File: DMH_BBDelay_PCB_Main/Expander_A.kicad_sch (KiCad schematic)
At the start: 23 parts, among them U27 SSI2162, U28 TL074

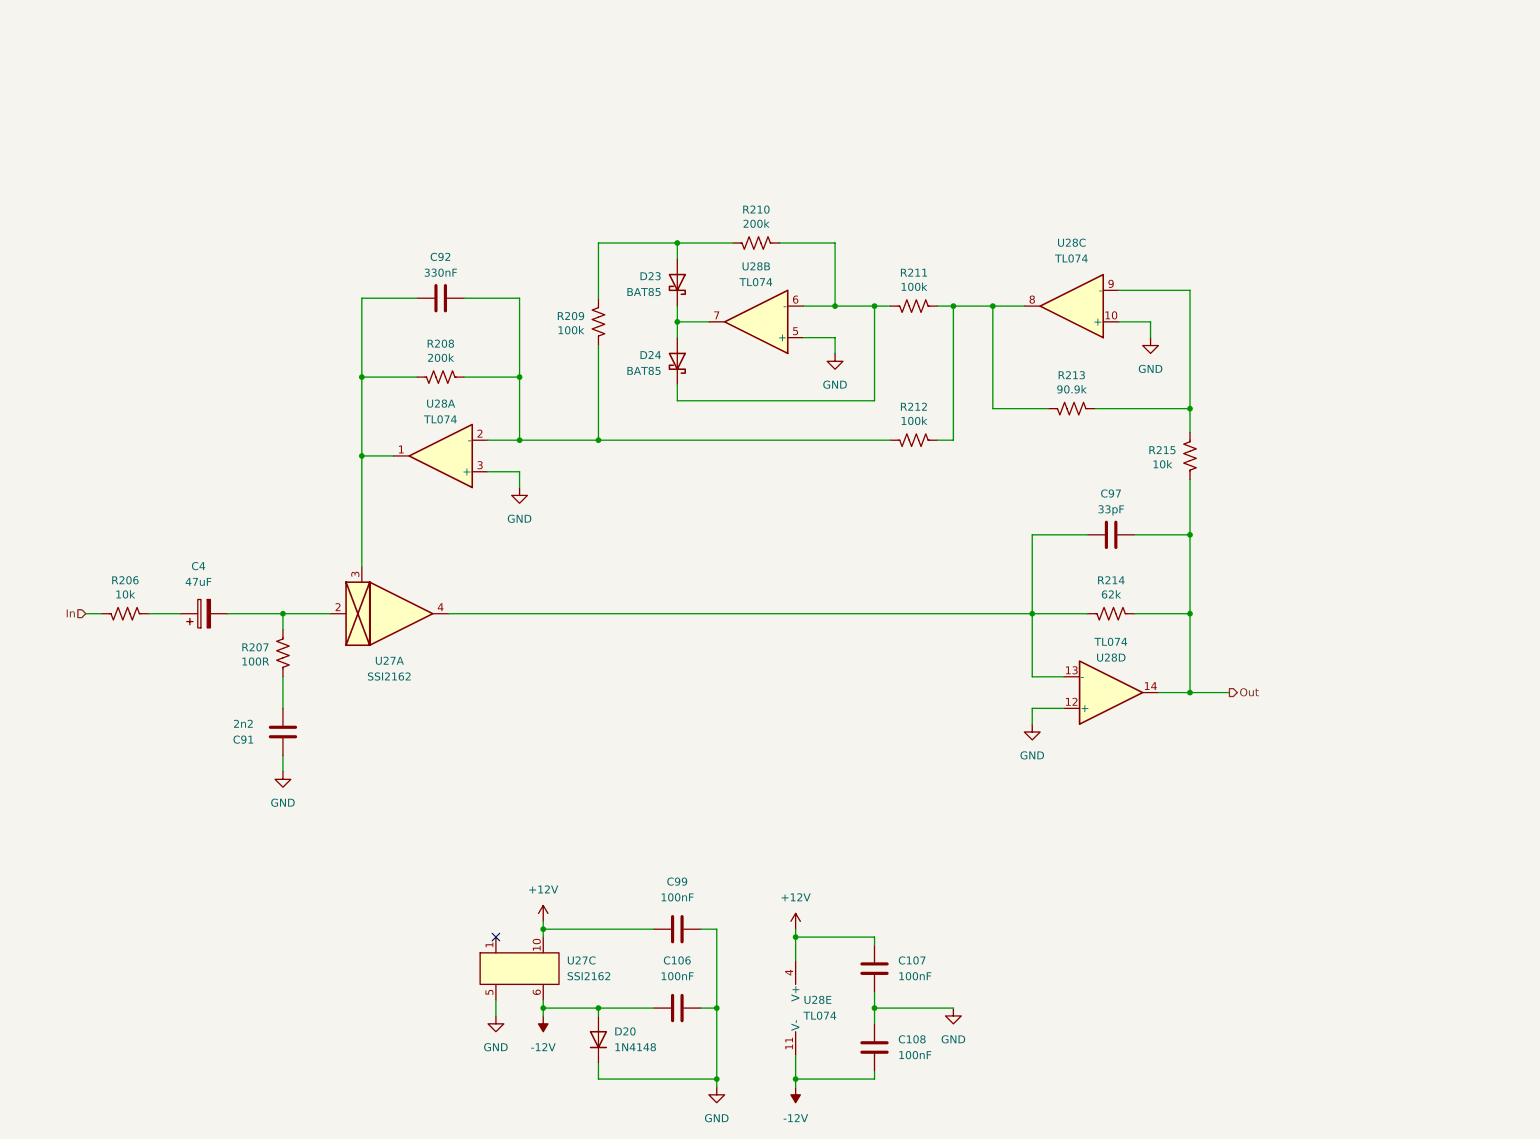
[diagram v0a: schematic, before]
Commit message: Designed Expander circuits
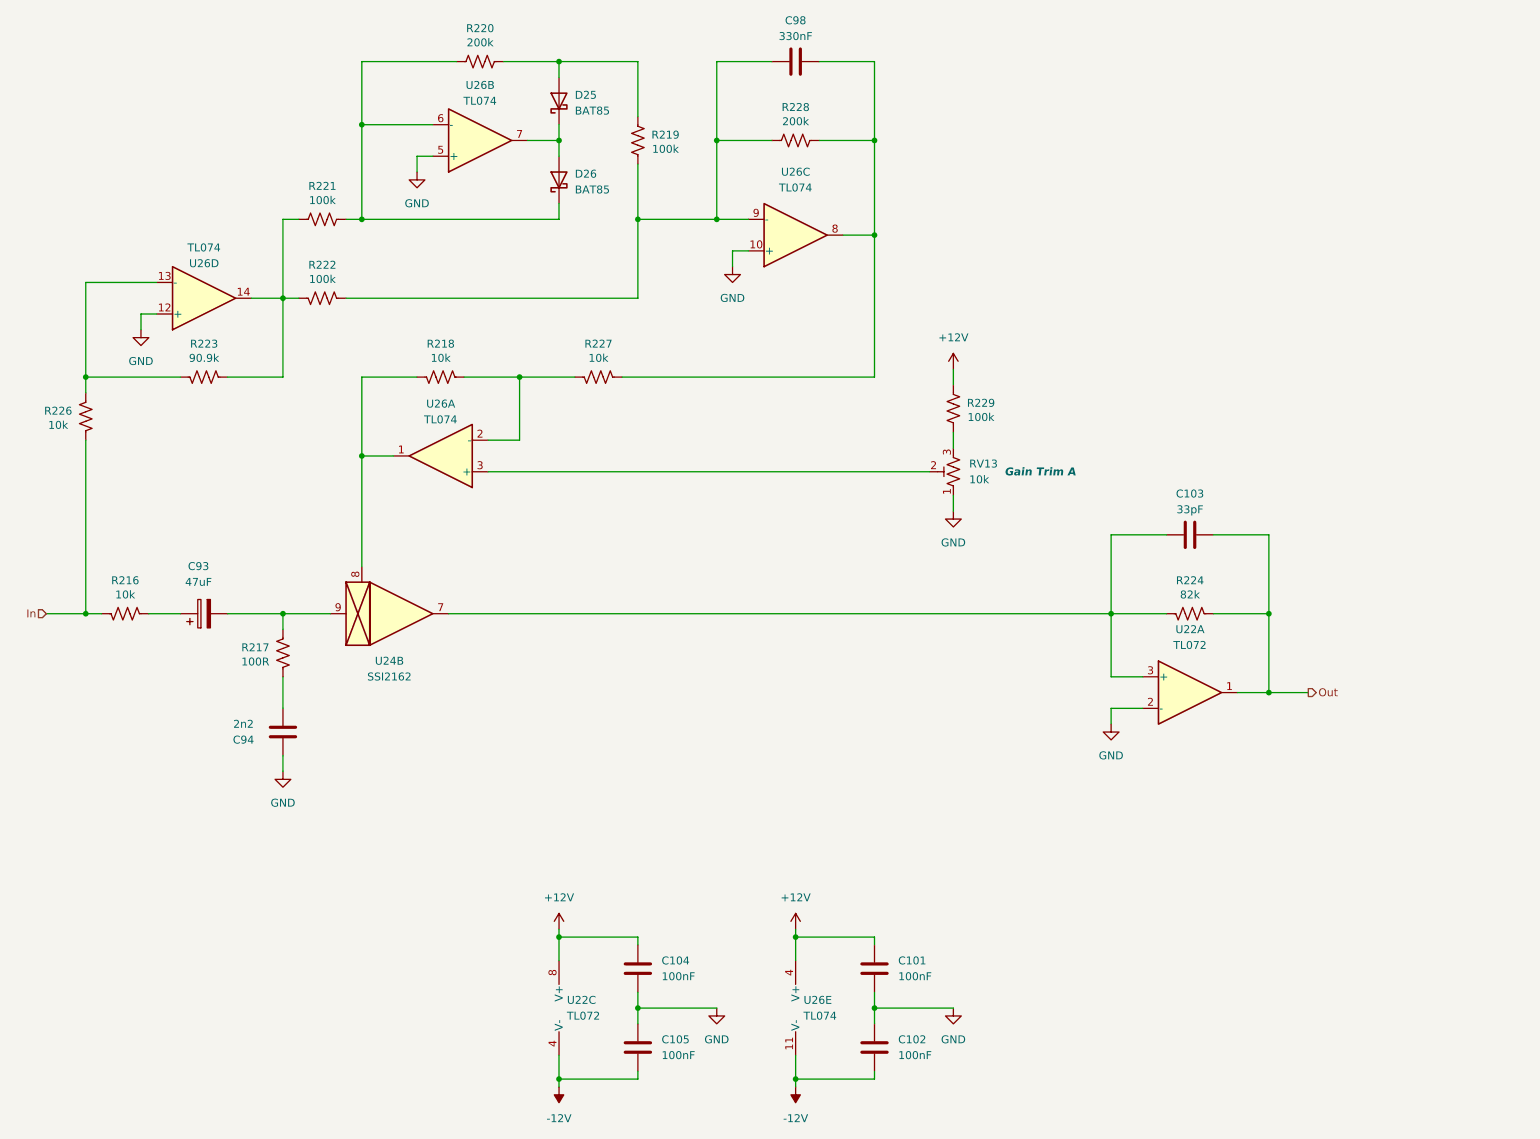
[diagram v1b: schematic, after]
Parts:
- removed C106, C107, C108, C99: 100nF, Capacitor_THT:C_Disc_D4.3mm_W1.9mm_P5.00mm, symbol Device:C
- removed D20: 1N4148, Diode_THT:D_DO-35_SOD27_P7.62mm_Horizontal, symbol Diode:1N4148
- removed R213: 90.9k, Resistor_THT:R_Axial_DIN0207_L6.3mm_D2.5mm_P7.62mm_Horizontal, symbol Device:R_US
- removed R215: 10k, Resistor_THT:R_Axial_DIN0207_L6.3mm_D2.5mm_P7.62mm_Horizontal, symbol Device:R_US
- removed U27: SSI2162, Package_SO:SSOP-10_3.9x4.9mm_P1.00mm, symbol SynthStuff:SSI2162
- removed unit 4 of U28
- added C101, C102, C104, C105: 100nF, Capacitor_THT:C_Disc_D4.3mm_W1.9mm_P5.00mm, symbol Device:C
- added R223: 90.9k, Resistor_THT:R_Axial_DIN0207_L6.3mm_D2.5mm_P7.62mm_Horizontal, symbol Device:R_US
- added R226, R227: 10k, Resistor_THT:R_Axial_DIN0207_L6.3mm_D2.5mm_P7.62mm_Horizontal, symbol Device:R_US
- added R228: 200k, Resistor_THT:R_Axial_DIN0207_L6.3mm_D2.5mm_P7.62mm_Horizontal, symbol Device:R_US
- added R229: 100k, Resistor_THT:R_Axial_DIN0207_L6.3mm_D2.5mm_P7.62mm_Horizontal, symbol Device:R_US
- added RV13: 10k, Potentiometer_THT:Potentiometer_Bourns_3296X_Horizontal, symbol Device:R_Potentiometer_Trim_US
- added U22: TL072, Package_DIP:DIP-8_W7.62mm_Socket, symbol Amplifier_Operational:TL072
- added U24: SSI2162, Package_SO:SSOP-10_3.9x4.9mm_P1.00mm, symbol SynthStuff:SSI2162
- added unit 4 of U26
- R218: renamed from R208; value 200k -> 10k
- R224: renamed from R214; value 62k -> 82k
- renumbered C97 to C103, C4 to C93, C91 to C94, C92 to C98, D23 to D25, D24 to D26, R206 to R216, R207 to R217, R209 to R219, R210 to R220, R211 to R221, R212 to R222, U28 to U26
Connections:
- net +12V: now also C101.1, C104.1, R229.2, U22.8 (V+)
- net -12V: now also C102.2, C105.2, U22.4 (V-)
- net GND: now also C101.2, C102.1, C104.2, C105.1, RV13.1, U22.2 (-), U26.12 (+); no longer U26.3 (+)
- net In: now also R226.1
- net Out: now also U22.1
- net at U26.9 (-): now also C98.1, R219.1, R222.2, R228.2
- net at R218.1, U26.1: now also U24.8 (Vc_2); no longer C98.1
- net at C103.1, R224.1: now also U22.3 (+), U24.7 (Out_2)
- net at C93.2, R217.2: now also U24.9 (In_2)
- new net: C98.2, R227.2, R228.1, U26.8
- new net: R218.2, R227.1, U26.2 (-)
- new net: RV13.2, U26.3 (+)
- new net: R223.1, R226.2, U26.13 (-)
- new net: R221.2, R222.1, R223.2, U26.14
- new net: R229.1, RV13.3
- no-connect marks 1 -> 0
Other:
- moved on the sheet: C103, C98, D25, D26, R219, R220, R221, R222, R224, U26B, U26C

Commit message: Fixed mistake with expander output opamp
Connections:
- net GND: now also U22.3 (+); no longer U22.2 (-)
- net at C103.1, R224.1, U24.7 (Out_2): now also U22.2 (-); no longer U22.3 (+)
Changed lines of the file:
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@@
 		(lib_id "Amplifier_Operational:TL072")
 		(at 203.2 127 0)
+		(mirror x)
 		(unit 1)
 		(body_style 1)
@@
 		(in_pos_files yes)
 		(dnp no)
-		(fields_autoplaced yes)
 		(property "Reference" "U22"
-			(at 203.2 116.84 0)
+			(at 203.2 137.16 0)
 			(show_name no)
 			(do_not_autoplace no)
@@
 		)
 		(property "Value" "TL072"
-			(at 203.2 119.38 0)
+			(at 203.2 134.62 0)
 			(show_name no)
 			(do_not_autoplace no)

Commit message: Added notes from troubleshooting
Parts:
- R228: value 200k -> 120k
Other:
- note added: "The attack time of this expader is way too slow for a decent plucky delay effect, but reducing the 330nF cap distorts the signal heavily. Reducing R228 from 200k to 120k helped The loos in expansion could be easily compensated with RV13."
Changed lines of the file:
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@@
 		(comment 1 "PCB for 10cm Kosmo format synthesizer module")
 	)
+	(circle
+		(center 139.7 35.56)
+		(radius 6.35)
+		(stroke
+			(width 0)
+			(type default)
+		)
+		(fill
+			(type none)
+		)
+	)
+	(text "The attack time of this expader is way too slow for a decent plucky\ndelay effect, but reducing the 330nF cap distorts the signal heavily.\nReducing R228 from 200k to 120k helped\nThe loos in expansion could be easily compensated with RV13."
+		(exclude_from_sim no)
+		(at 188.468 33.528 0)
+		(effects
+			(font
+				(size 1.27 1.27)
+			)
+		)
+	)
 	(junction
 		(at 127 38.1)
@@
 			)
 		)
-		(property "Value" "200k"
+		(property "Value" "120k"
 			(at 139.7 35.052 90)
 			(show_name no)

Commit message: Tweaked compander
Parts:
- C94: now not fitted
- R217: value 100R -> 1k
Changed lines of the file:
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@@
 			)
 		)
-		(property "Value" "100R"
+		(property "Value" "1k"
 			(at 52.705 122.047 0)
 			(show_name no)
@@
 		(on_board yes)
 		(in_pos_files yes)
-		(dnp no)
+		(dnp yes)
 		(property "Reference" "C94"
 			(at 50.8 134.62 0)

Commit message: Scaled up components in Tone Control part
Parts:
- R228: value 120k -> 100k
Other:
- note added: "Changed resistor from 100R to 1k, and replaced 2n2 with short"
- note added: "The attack time of this expader is way too slow for a decent plucky delay effect, but reducing the 330nF cap distorts the signal heavily. Reducing R228 from 200k to 100k helped The loos in expansion could be easily compensated with RV13."
- note removed: "The attack time of this expader is way too slow for a decent plucky delay effect, but reducing the 330nF cap distorts the signal heavily. Reducing R228 from 200k to 120k helped The loos in expansion could be easily compensated with RV13."
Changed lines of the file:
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@@
 		)
 	)
-	(text "The attack time of this expader is way too slow for a decent plucky\ndelay effect, but reducing the 330nF cap distorts the signal heavily.\nReducing R228 from 200k to 120k helped\nThe loos in expansion could be easily compensated with RV13."
+	(circle
+		(center 54.61 120.65)
+		(radius 5.08)
+		(stroke
+			(width 0)
+			(type default)
+		)
+		(fill
+			(type none)
+		)
+	)
+	(text "The attack time of this expader is way too slow for a decent plucky\ndelay effect, but reducing the 330nF cap distorts the signal heavily.\nReducing R228 from 200k to 100k helped\nThe loos in expansion could be easily compensated with RV13."
 		(exclude_from_sim no)
 		(at 188.468 33.528 0)
@@
 		)
 	)
+	(text "Changed resistor from 100R to 1k,\nand replaced 2n2 with short"
+		(exclude_from_sim no)
+		(at 34.036 128.778 0)
+		(effects
+			(font
+				(size 1.27 1.27)
+			)
+		)
+	)
 	(junction
 		(at 127 38.1)
@@
 			)
 		)
-		(property "Value" "120k"
+		(property "Value" "100k"
 			(at 139.7 35.052 90)
 			(show_name no)

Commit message: Made feedback work
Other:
- note added: "Try adding zener limiting here"
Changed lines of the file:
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@@
+		)
+	)
+	(text "Try adding zener limiting here"
+		(exclude_from_sim no)
+		(at 229.616 133.858 0)
+		(effects
+			(font
+				(size 1.27 1.27)
+			)
 		)
 	)

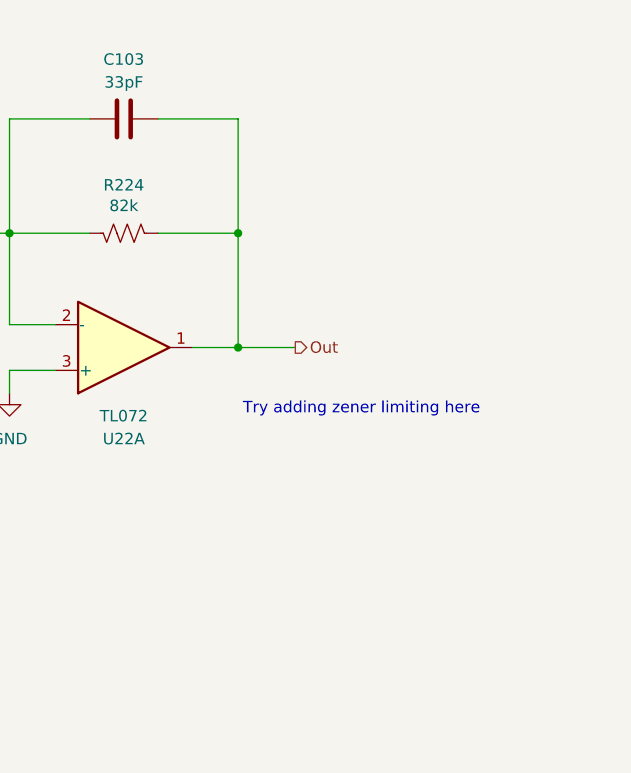
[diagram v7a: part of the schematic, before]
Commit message: Removed compander and adjusted feedback
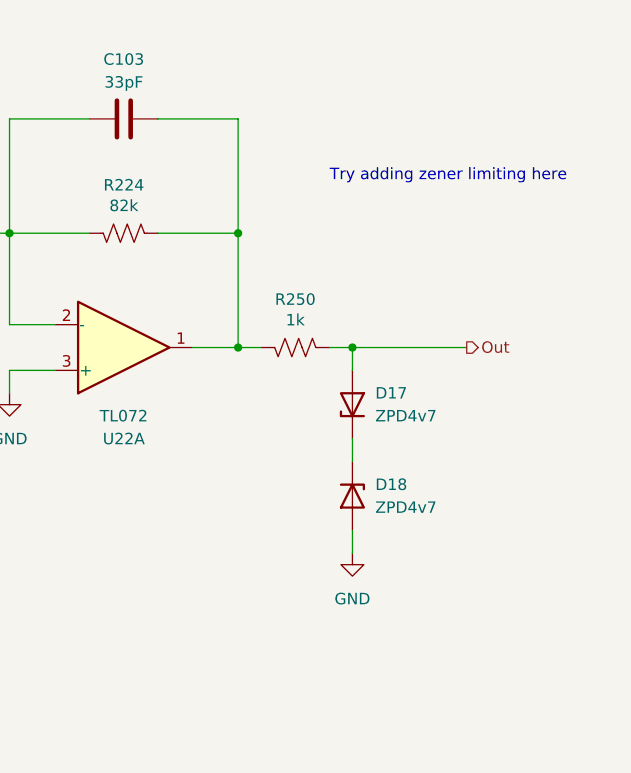
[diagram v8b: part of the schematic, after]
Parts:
- added D17, D18: ZPD4v7, Diode_THT:D_DO-35_SOD27_P7.62mm_Horizontal, symbol Diode:ZPDxx
- added R250: 1k, Resistor_THT:R_Axial_DIN0207_L6.3mm_D2.5mm_P7.62mm_Horizontal, symbol Device:R_US
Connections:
- net GND: now also D18.2 (A)
- net Out: now also D17.2 (A), R250.2; no longer C103.2, R224.2, U22.1
- new net: C103.2, R224.2, R250.1, U22.1
- new net: D17.1 (K), D18.1 (K)
